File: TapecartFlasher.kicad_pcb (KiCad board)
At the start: 2 copper layers, 26.9 x 59.8 mm, 17 parts, among them J1 C64-CassettePort, J2 SD Module, P1 Digital, P2 Analog, Q1 BC547, Q2 BC557

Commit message: Project address should have been on there.
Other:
- board text added: "github.com/hackup/TapecartFlasherNano"
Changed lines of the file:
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@@
   (general
     (thickness 1.6)
-    (drawings 32)
+    (drawings 33)
     (tracks 186)
     (zones 0)
@@
     (38 B.Mask user)
     (39 F.Mask user)
-    (40 Dwgs.User user hide)
+    (40 Dwgs.User user)
     (41 Cmts.User user)
     (42 Eco1.User user)
@@
     )
   )
+  (gr_text github.com/hackup/TapecartFlasherNano (at 152.273 92.329 90) (layer B.SilkS)
+    (effects (font (size 1 1) (thickness 0.2)) (justify mirror))
+  )
   (gr_text Rev.1 (at 163.83 109.982) (layer F.SilkS)

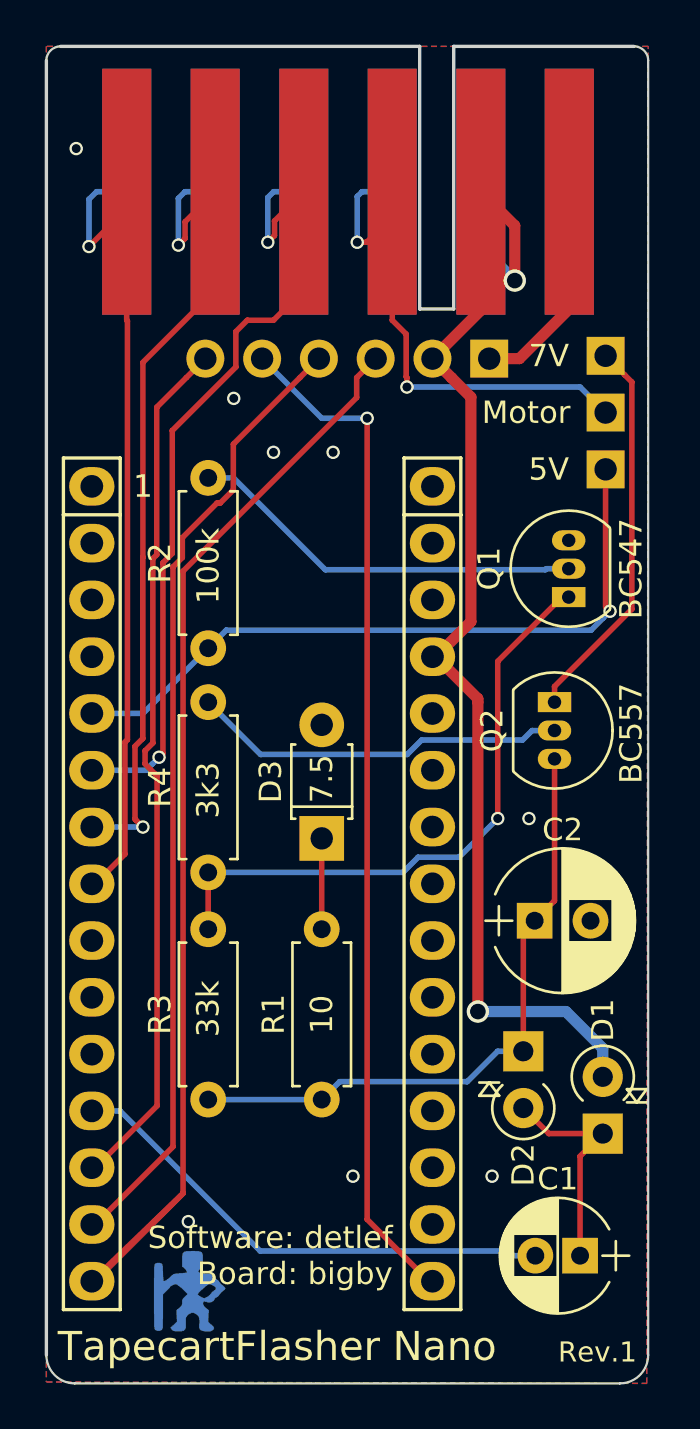
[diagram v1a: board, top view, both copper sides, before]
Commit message: Changed resistor footprints.
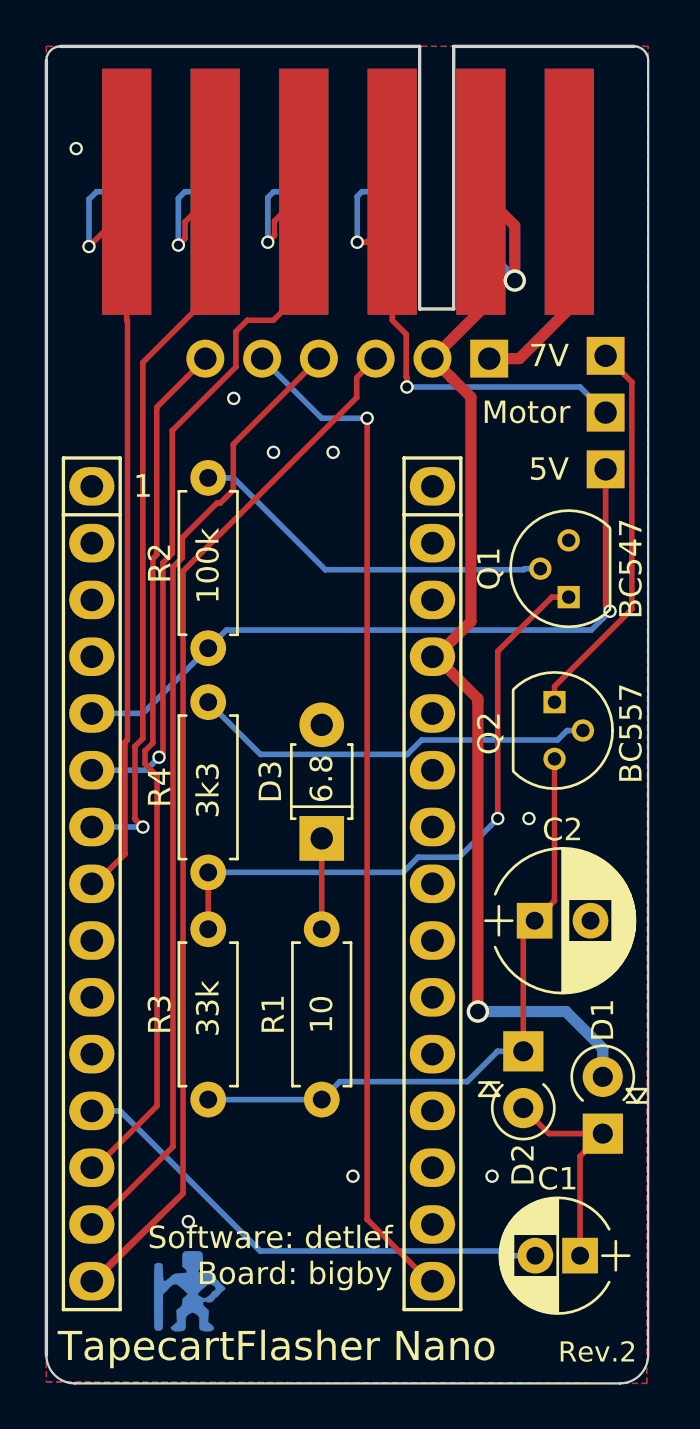
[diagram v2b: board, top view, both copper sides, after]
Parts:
- D3: value 7.5 -> 6.8
- Q1, Q2: footprint TO_SOT_Packages_THT:TO-92_Inline_Narrow_Oval -> TO_SOT_Packages_THT:TO-92_Molded_Narrow
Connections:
- P1 pad 1: /1(Tx) -> (no net)
- P1 pad 10: /7 -> (no net)
- P1 pad 11: /8 -> (no net)
- P1 pad 2: /0(Rx) -> (no net)
- P1 pad 3: /Reset -> (no net)
- P1 pad 9: /6(**) -> (no net)
- P2 pad 1: /Vin -> (no net)
- P2 pad 10: /A2 -> (no net)
- P2 pad 11: /A1 -> (no net)
- P2 pad 12: /A0 -> (no net)
- P2 pad 13: /AREF -> (no net)
- P2 pad 14: +3V3 -> (no net)
- P2 pad 3: /RST -> (no net)
- P2 pad 5: /A7 -> (no net)
- P2 pad 6: /A6 -> (no net)
- P2 pad 7: /A5 -> (no net)
- P2 pad 8: /A4 -> (no net)
- P2 pad 9: /A3 -> (no net)
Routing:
- net Net-(Q2-Pad2): track 16.9 -> 18.2 mm
- net Net-(Q1-Pad2): track 17.9 -> 16.6 mm
- net Net-(Q1-Pad1): track 27.9 -> 28.5 mm
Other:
- board text added: "Rev.2"
- board text removed: "Rev.1"

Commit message: Modified/corrected zender diode circuit.
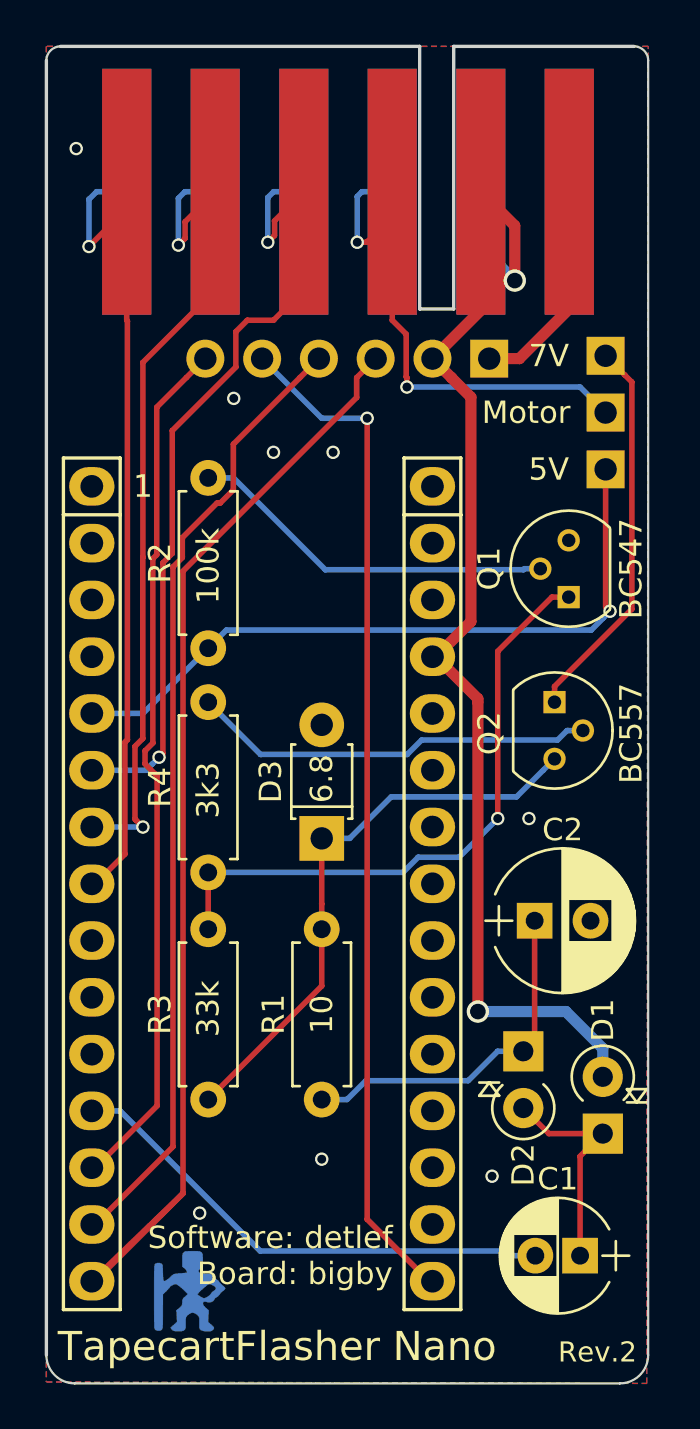
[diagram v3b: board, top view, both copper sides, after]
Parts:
- moved R1 7.62 mm to (149.7, 98.7), turned to 90 degrees
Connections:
- C2 pad 1: VPP -> Net-(C2-Pad1)
- D2 pad 1: VPP -> Net-(C2-Pad1)
- D3 pad 1: Net-(D3-Pad1) -> VPP
- P1 pad 1: (no net) -> /1(Tx)
- P1 pad 10: (no net) -> /7
- P1 pad 11: (no net) -> /8
- P1 pad 2: (no net) -> /0(Rx)
- P1 pad 3: (no net) -> /Reset
- P1 pad 9: (no net) -> /6(**)
- P2 pad 1: (no net) -> /Vin
- P2 pad 10: (no net) -> /A2
- P2 pad 11: (no net) -> /A1
- P2 pad 12: (no net) -> /A0
- P2 pad 13: (no net) -> /AREF
- P2 pad 14: (no net) -> +3V3
- P2 pad 3: (no net) -> /RST
- P2 pad 5: (no net) -> /A7
- P2 pad 6: (no net) -> /A6
- P2 pad 7: (no net) -> /A5
- P2 pad 8: (no net) -> /A4
- P2 pad 9: (no net) -> /A3
- R1 pad 1: Net-(D3-Pad1) -> Net-(C2-Pad1)
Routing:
- net Net-(C2-Pad1): track 0.00 -> 16.0 mm
- net Net-(D3-Pad1): track 4.06 -> 0.00 mm
- net VPP: track 28.7 -> 25.7 mm

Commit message: Added decoupling capacitor to prevent Arduino from rebooting.
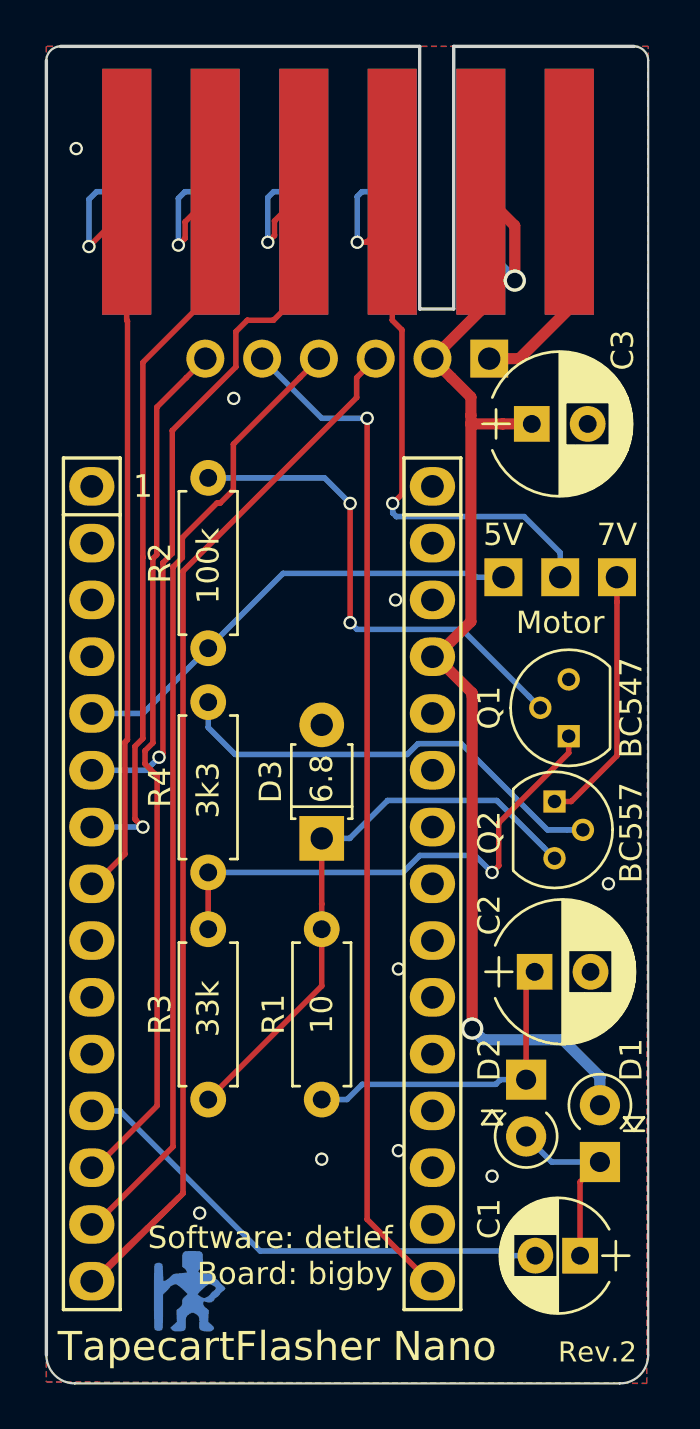
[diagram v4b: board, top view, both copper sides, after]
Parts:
- added C3: 220µ, Capacitors_THT:CP_Radial_D6.3mm_P2.50mm, F.Cu at (159.1, 68.5)
- moved JP1 6.65 mm to (157.9, 75.3), turned to 90 degrees
- moved Q1 6.22 mm to (160.8, 82.4)
- moved Q2 4.44 mm to (160.1, 85.3)
- moved C2 2.29 mm to (159.3, 93.0)
- moved D2 1.28 mm to (158.9, 97.8)
- moved D1 1.28 mm to (162.2, 101.5)
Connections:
- P1 pad 1: /1(Tx) -> (no net)
- P1 pad 10: /7 -> (no net)
- P1 pad 11: /8 -> (no net)
- P1 pad 2: /0(Rx) -> (no net)
- P1 pad 3: /Reset -> (no net)
- P1 pad 9: /6(**) -> (no net)
- P2 pad 1: /Vin -> (no net)
- P2 pad 10: /A2 -> (no net)
- P2 pad 11: /A1 -> (no net)
- P2 pad 12: /A0 -> (no net)
- P2 pad 13: /AREF -> (no net)
- P2 pad 14: +3V3 -> (no net)
- P2 pad 3: /RST -> (no net)
- P2 pad 5: /A7 -> (no net)
- P2 pad 6: /A6 -> (no net)
- P2 pad 7: /A5 -> (no net)
- P2 pad 8: /A4 -> (no net)
- P2 pad 9: /A3 -> (no net)
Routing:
- net Motor5: track 31.5 -> 21.1 mm, vias 1 -> 0
- net Motor7: track 17.4 -> 11.6 mm
- net Net-(J1-Pad3): track 25.2 -> 30.9 mm
- net Net-(Q1-Pad2): track 16.6 -> 22.2 mm, vias 0 -> 2
- net Net-(Q1-Pad1): track 28.5 -> 23.4 mm
- net +5V: track 56.6 -> 60.3 mm
- net Net-(Q2-Pad2): track 18.2 -> 20.2 mm
- net Net-(C1-Pad1): track 9.91 -> 8.33 mm
- net Net-(C2-Pad1): track 16.0 -> 14.5 mm
- net GND: vias 8 -> 9

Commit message: Fixed gold fingers.
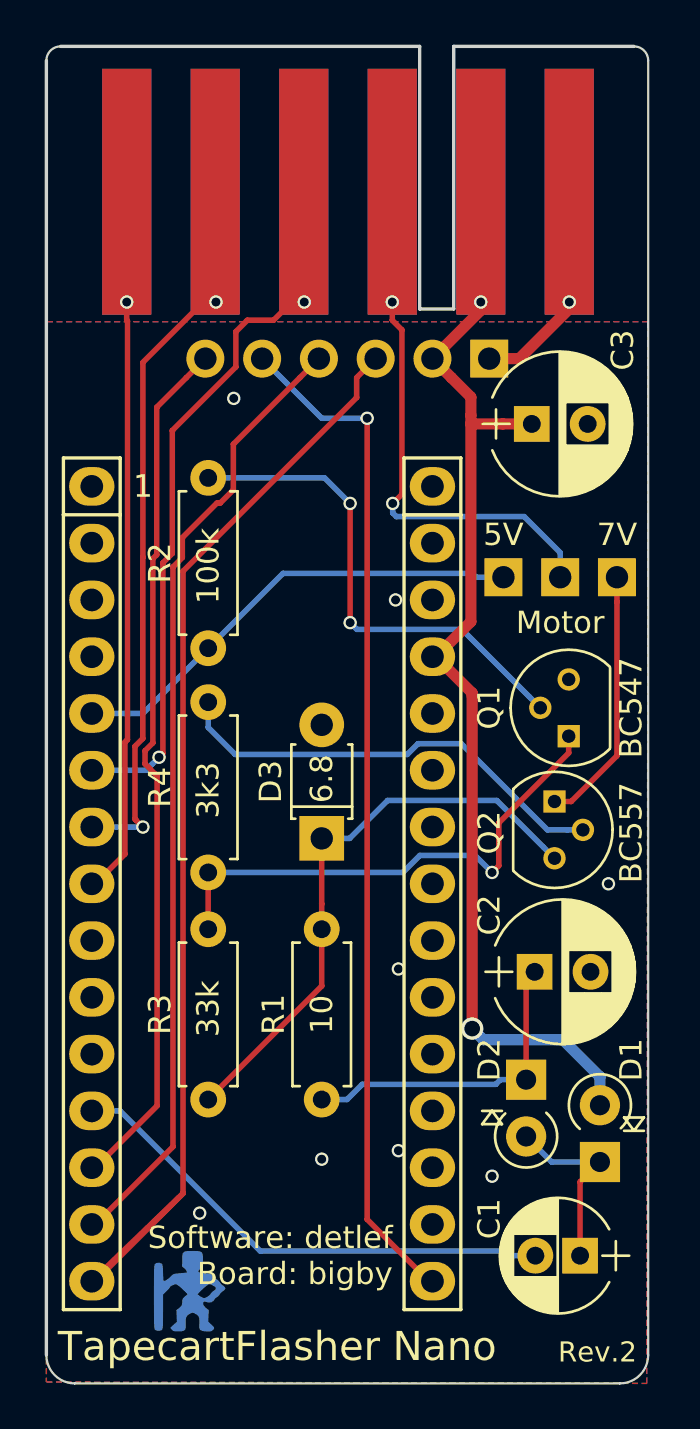
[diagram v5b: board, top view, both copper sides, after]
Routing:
- net +5V: track 60.3 -> 51.1 mm
- net Sense: track 38.8 -> 31.7 mm
- net Write: track 39.3 -> 32.3 mm
- net Net-(J1-Pad3): track 30.9 -> 24.0 mm
- net Read: track 38.6 -> 31.9 mm

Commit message: Moved switch labels.
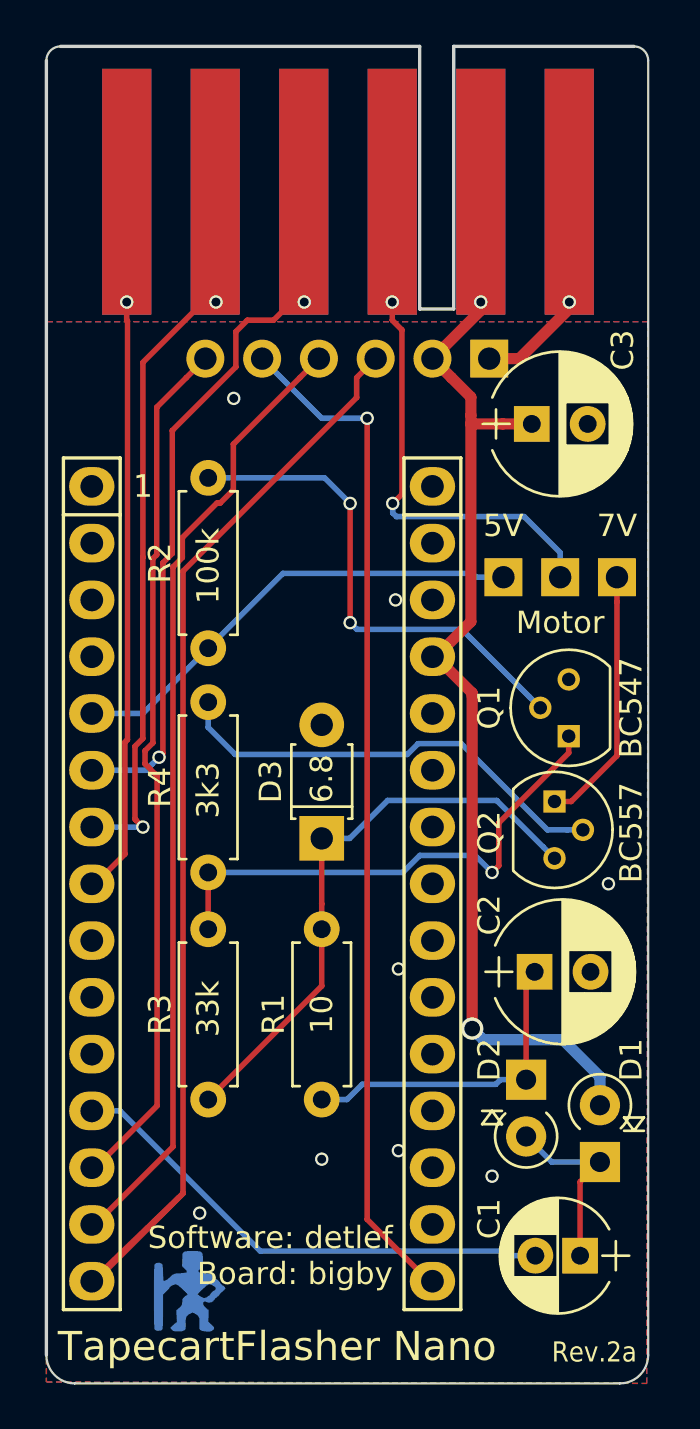
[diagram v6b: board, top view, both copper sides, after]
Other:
- board text added: "Rev.2a"
- board text removed: "Rev.2"
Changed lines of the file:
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@@
   (title_block
     (title "TapecartFlasher Nano")
-    (date 2018-09-06)
-    (rev Rev.2)
+    (date 2018-12-04)
+    (rev Rev.2a)
     (company hackup.net)
   )
@@
     (effects (font (size 1 1) (thickness 0.2)) (justify mirror))
   )
-  (gr_text Rev.2 (at 163.83 109.982) (layer F.SilkS)
-    (effects (font (size 0.9 0.9) (thickness 0.18)) (justify right))
+  (gr_text Rev.2a (at 163.83 109.982) (layer F.SilkS)
+    (effects (font (size 0.9 0.8) (thickness 0.18)) (justify right))
   )
   (gr_text CS (at 144.526 67.437 90) (layer B.SilkS)
@@
     (effects (font (size 1 1) (thickness 0.2)))
   )
-  (gr_text 5V (at 157.861 73.406) (layer F.SilkS)
+  (gr_text 5V (at 157.861 73.006) (layer F.SilkS)
     (effects (font (size 1 1) (thickness 0.2)))
   )
-  (gr_text 7V (at 162.941 73.406) (layer F.SilkS)
+  (gr_text 7V (at 162.941 73.006) (layer F.SilkS)
     (effects (font (size 1 1) (thickness 0.2)))
   )
@@
   (gr_line (start 143.51 112.522) (end 150.622 112.522) (angle 90) (layer Dwgs.User) (width 0.15))
   (gr_line (start 143.51 110.617) (end 143.51 112.522) (angle 90) (layer Dwgs.User) (width 0.15))
-  (via (at 148.95 63) (size 0.6) (drill 0.4) (layers F.Cu B.Cu) (net 8))
-  (via (at 145 63) (size 0.6) (drill 0.4) (layers F.Cu B.Cu) (net 7))
   (via (at 149.733 101.346) (size 0.6) (drill 0.4) (layers F.Cu B.Cu) (net 1))
   (via (at 145.796 67.31) (size 0.6) (drill 0.4) (layers F.Cu B.Cu) (net 1))
@@
   (segment (start 141.008 62.85) (end 141.008 63.8135) (width 0.25) (layer F.Cu) (net 6) (status 10))
   (via (at 141.008 63) (size 0.6) (drill 0.4) (layers F.Cu B.Cu) (net 6))
+  (via (at 145 63) (size 0.6) (drill 0.4) (layers F.Cu B.Cu) (net 7))
   (via (at 141.732 86.487) (size 0.6) (drill 0.4) (layers F.Cu B.Cu) (net 7))
   (segment (start 141.732 86.487) (end 139.446 86.487) (width 0.25) (layer B.Cu) (net 7) (status 20))
@@
   (segment (start 141.732 65.6995) (end 141.732 74.416356) (width 0.25) (layer F.Cu) (net 7))
   (segment (start 141.727955 82.528146) (end 141.377965 82.878136) (width 0.25) (layer F.Cu) (net 7))
+  (via (at 148.95 63) (size 0.6) (drill 0.4) (layers F.Cu B.Cu) (net 8))
   (segment (start 141.870516 83.947) (end 142.152979 83.664537) (width 0.25) (layer B.Cu) (net 8))
   (segment (start 142.627977 74.666201) (end 142.627977 83.189539) (width 0.25) (layer F.Cu) (net 8))
